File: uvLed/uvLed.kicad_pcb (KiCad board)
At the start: 2 copper layers, 71 x 9 mm, 7 parts, among them J1 Conn_01x02

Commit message: insert C
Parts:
- added C1: 100n, Capacitor_SMD:C_0805_2012Metric_Pad1.18x1.45mm_HandSolder, F.Cu at (128.7, 74.3)
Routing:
- net Net-(D4-A): track 9.19 -> 9.80 mm
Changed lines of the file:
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@@
+    )
+  )
+  (footprint "Capacitor_SMD:C_0805_2012Metric_Pad1.18x1.45mm_HandSolder" (layer "F.Cu")
+    (at 128.7 74.2625 -90)
+    (descr "Capacitor SMD 0805 (2012 Metric), square (rectangular) end terminal, IPC_7351 nominal with elongated pad for handsoldering. (Body size source: IPC-SM-782 page 76, https://www.pcb-3d.com/wordpress/wp-content/uploads/ipc-sm-782a_amendment_1_and_2.pdf, https://docs.google.com/spreadsheets/d/1BsfQQcO9C6DZCsRaXUlFlo91Tg2WpOkGARC1WS5S8t0/edit?usp=sharing), generated with kicad-footprint-generator")
+    (tags "capacitor handsolder")
+    (property "Sheetfile" "uvLed.kicad_sch")
+    (property "Sheetname" "")
+    (property "ki_description" "Unpolarized capacitor")
+    (property "ki_keywords" "cap capacitor")
+    (attr smd)
+    (fp_text reference "C1" (at 0 -1.68 90) (layer "F.SilkS")
+        (effects (font (size 1 1) (thickness 0.15)))
+    )
+    (fp_text value "100n" (at 0 1.68 90) (layer "F.Fab")
+        (effects (font (size 1 1) (thickness 0.15)))
+    )
+    (fp_text user "${REFERENCE}" (at 0 0 90) (layer "F.Fab")
+        (effects (font (size 0.5 0.5) (thickness 0.08)))
+    )
+    (fp_line (start -0.261252 -0.735) (end 0.261252 -0.735)
+      (stroke (width 0.12) (type solid)) (layer "F.SilkS"))
+    (fp_line (start -0.261252 0.735) (end 0.261252 0.735)
+      (stroke (width 0.12) (type solid)) (layer "F.SilkS"))
+    (fp_line (start -1.88 -0.98) (end 1.88 -0.98)
+      (stroke (width 0.05) (type solid)) (layer "F.CrtYd"))
+    (fp_line (start -1.88 0.98) (end -1.88 -0.98)
+      (stroke (width 0.05) (type solid)) (layer "F.CrtYd"))
+    (fp_line (start 1.88 -0.98) (end 1.88 0.98)
+      (stroke (width 0.05) (type solid)) (layer "F.CrtYd"))
+    (fp_line (start 1.88 0.98) (end -1.88 0.98)
+      (stroke (width 0.05) (type solid)) (layer "F.CrtYd"))
+    (fp_line (start -1 -0.625) (end 1 -0.625)
+      (stroke (width 0.1) (type solid)) (layer "F.Fab"))
+    (fp_line (start -1 0.625) (end -1 -0.625)
+      (stroke (width 0.1) (type solid)) (layer "F.Fab"))
+    (fp_line (start 1 -0.625) (end 1 0.625)
+      (stroke (width 0.1) (type solid)) (layer "F.Fab"))
+    (fp_line (start 1 0.625) (end -1 0.625)
+      (stroke (width 0.1) (type solid)) (layer "F.Fab"))
+    (pad "1" smd roundrect (at -1.0375 0 270) (size 1.175 1.45) (layers "F.Cu" "F.Paste" "F.Mask") (roundrect_rratio 0.212766)
+      (net 5 "Net-(D4-A)") (pintype "passive"))
+    (pad "2" smd roundrect (at 1.0375 0 270) (size 1.175 1.45) (layers "F.Cu" "F.Paste" "F.Mask") (roundrect_rratio 0.212766)
+      (net 2 "GND") (pintype "passive"))
+    (model "${KICAD6_3DMODEL_DIR}/Capacitor_SMD.3dshapes/C_0805_2012Metric.wrl"
+      (offset (xyz 0 0 0))
+      (scale (xyz 1 1 1))
+      (rotate (xyz 0 0 0))
     )
   )
@@
   (segment (start 124 75.3) (end 119 75.3) (width 0.8) (layer "F.Cu") (net 4))
   (segment (start 116.7 73) (end 112 73) (width 0.8) (layer "F.Cu") (net 4))
+  (segment (start 128.575 73.1) (end 128.7 73.225) (width 0.5) (layer "F.Cu") (net 5))
   (segment (start 133 73.46) (end 132.54 73) (width 0.8) (layer "F.Cu") (net 5))
-  (segment (start 132.54 73) (end 124 73) (width 0.8) (layer "F.Cu") (net 5))
+  (segment (start 133 73.46) (end 132.765 73.225) (width 0.8) (layer "F.Cu") (net 5))
+  (segment (start 124 73.1) (end 128.575 73.1) (width 0.5) (layer "F.Cu") (net 5))
+  (segment (start 132.765 73.225) (end 128.7 73.225) (width 0.8) (layer "F.Cu") (net 5))
   (zone (net 2) (net_name "GND") (layer "F.Cu") (hatch edge 0.5)
     (connect_pads (clearance 0.8))

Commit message: change pcb
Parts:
- moved D4 14.4 mm to (138.4, 74.0)
- moved C1 12.6 mm to (141.3, 74.2)
- moved J1 11.3 mm to (144.3, 72.9)
- moved REF** 11.0 mm to (149.0, 74.0)
- moved D3 7.70 mm to (119.7, 74.2)
- moved D2 5.90 mm to (101.9, 74.2)
- moved D1 2.10 mm to (83.1, 74.0)
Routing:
- net Net-(D3-A): track 13.0 -> 19.5 mm
- net Net-(D1-A): track 15.9 -> 19.8 mm
- net Net-(D4-A): track 9.80 -> 6.01 mm
- net Net-(D2-A): track 17.0 -> 18.7 mm
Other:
- board size 71 x 9 mm -> 81.9 x 9 mm
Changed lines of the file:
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@@
   (net 5 "Net-(D4-A)")
   (footprint "uvLED:SMD-2" (layer "F.Cu")
-    (at 124 74 90)
+    (at 138.4 74.05 90)
     (descr "LED SMD 2010 (5025 Metric), square (rectangular) end terminal, IPC_7351 nominal, (Body size source: http://www.tortai-tech.com/upload/download/2011102023233369053.pdf), generated with kicad-footprint-generator")
     (tags "LED")
@@
   )
   (footprint "MountingHole:MountingHole_2.5mm" (layer "F.Cu")
-    (at 138 74)
+    (at 149 74)
     (descr "Mounting Hole 2.5mm, no annular")
     (tags "mounting hole 2.5mm no annular")
@@
   )
   (footprint "uvLED:SMD-2" (layer "F.Cu")
-    (at 112 74 90)
+    (at 119.7 74.2 90)
     (descr "LED SMD 2010 (5025 Metric), square (rectangular) end terminal, IPC_7351 nominal, (Body size source: http://www.tortai-tech.com/upload/download/2011102023233369053.pdf), generated with kicad-footprint-generator")
     (tags "LED")
@@
   )
   (footprint "Capacitor_SMD:C_0805_2012Metric_Pad1.18x1.45mm_HandSolder" (layer "F.Cu")
-    (at 128.7 74.2625 -90)
+    (at 141.3 74.15 -90)
     (descr "Capacitor SMD 0805 (2012 Metric), square (rectangular) end terminal, IPC_7351 nominal with elongated pad for handsoldering. (Body size source: IPC-SM-782 page 76, https://www.pcb-3d.com/wordpress/wp-content/uploads/ipc-sm-782a_amendment_1_and_2.pdf, https://docs.google.com/spreadsheets/d/1BsfQQcO9C6DZCsRaXUlFlo91Tg2WpOkGARC1WS5S8t0/edit?usp=sharing), generated with kicad-footprint-generator")
     (tags "capacitor handsolder")
@@
   )
   (footprint "uvLED:SMD-2" (layer "F.Cu")
-    (at 96 74 90)
+    (at 101.9 74.2 90)
     (descr "LED SMD 2010 (5025 Metric), square (rectangular) end terminal, IPC_7351 nominal, (Body size source: http://www.tortai-tech.com/upload/download/2011102023233369053.pdf), generated with kicad-footprint-generator")
     (tags "LED")
@@
   )
   (footprint "uvLED:SMD-2" (layer "F.Cu")
-    (at 81 74 90)
+    (at 83.1 74 90)
     (descr "LED SMD 2010 (5025 Metric), square (rectangular) end terminal, IPC_7351 nominal, (Body size source: http://www.tortai-tech.com/upload/download/2011102023233369053.pdf), generated with kicad-footprint-generator")
     (tags "LED")
@@
   )
   (footprint "Connector_PinHeader_2.54mm:PinHeader_1x02_P2.54mm_Vertical" (layer "F.Cu")
-    (at 133 73.46)
+    (at 144.3 72.875)
     (descr "Through hole straight pin header, 1x02, 2.54mm pitch, single row")
     (tags "Through hole pin header THT 1x02 2.54mm single row")
@@
   (gr_line (start 70 70) (end 141 70)
     (stroke (width 0.15) (type default)) (layer "F.SilkS"))
+  (gr_line (start 141 70) (end 151.95 70)
+    (stroke (width 0.15) (type default)) (layer "F.SilkS"))
   (gr_line (start 70 79) (end 70 70)
     (stroke (width 0.15) (type default)) (layer "F.SilkS"))
   (gr_line (start 141 79) (end 70 79)
     (stroke (width 0.15) (type default)) (layer "F.SilkS"))
-  (gr_line (start 141 70) (end 141 79)
+  (gr_line (start 151.95 70) (end 151.95 79)
+    (stroke (width 0.15) (type default)) (layer "F.SilkS"))
+  (gr_line (start 141 79) (end 151.95 79)
     (stroke (width 0.15) (type default)) (layer "F.SilkS"))
   (gr_line (start 70 79) (end 70 70)
@@
   (gr_line (start 70 70) (end 141 70)
     (stroke (width 0.1) (type default)) (layer "Edge.Cuts"))
+  (gr_line (start 151.95 79) (end 141 79)
+    (stroke (width 0.1) (type default)) (layer "Edge.Cuts"))
   (gr_line (start 141 79) (end 70 79)
     (stroke (width 0.1) (type default)) (layer "Edge.Cuts"))
-  (gr_line (start 141 70) (end 141 79)
-    (stroke (width 0.1) (type default)) (layer "Edge.Cuts"))
-  (segment (start 96 75.3) (end 89.4 75.3) (width 0.8) (layer "F.Cu") (net 1))
-  (segment (start 89.4 75.3) (end 87.2 73.1) (width 0.8) (layer "F.Cu") (net 1))
-  (segment (start 87.2 73.1) (end 81 73.1) (width 0.8) (layer "F.Cu") (net 1))
-  (segment (start 102.3 75.3) (end 100 73) (width 0.8) (layer "F.Cu") (net 3))
-  (segment (start 112 75.3) (end 102.3 75.3) (width 0.8) (layer "F.Cu") (net 3))
-  (segment (start 100 73) (end 96 73) (width 0.8) (layer "F.Cu") (net 3))
-  (segment (start 119 75.3) (end 116.7 73) (width 0.8) (layer "F.Cu") (net 4))
-  (segment (start 124 75.3) (end 119 75.3) (width 0.8) (layer "F.Cu") (net 4))
-  (segment (start 116.7 73) (end 112 73) (width 0.8) (layer "F.Cu") (net 4))
-  (segment (start 128.575 73.1) (end 128.7 73.225) (width 0.5) (layer "F.Cu") (net 5))
-  (segment (start 133 73.46) (end 132.54 73) (width 0.8) (layer "F.Cu") (net 5))
-  (segment (start 133 73.46) (end 132.765 73.225) (width 0.8) (layer "F.Cu") (net 5))
-  (segment (start 124 73.1) (end 128.575 73.1) (width 0.5) (layer "F.Cu") (net 5))
-  (segment (start 132.765 73.225) (end 128.7 73.225) (width 0.8) (layer "F.Cu") (net 5))
+  (gr_line (start 151.95 70) (end 141 70)
+    (stroke (width 0.1) (type default)) (layer "Edge.Cuts"))
+  (gr_line (start 151.95 70) (end 151.95 79)
+    (stroke (width 0.1) (type default)) (layer "Edge.Cuts"))
+  (segment (start 90.4 73.1) (end 92.8 75.5) (width 0.5) (layer "F.Cu") (net 1))
+  (segment (start 92.8 75.5) (end 101.9 75.5) (width 0.5) (layer "F.Cu") (net 1))
+  (segment (start 83.1 73.1) (end 90.4 73.1) (width 0.5) (layer "F.Cu") (net 1))
+  (segment (start 111.75 75.5) (end 119.7 75.5) (width 0.5) (layer "F.Cu") (net 3))
+  (segment (start 101.9 73.3) (end 109.55 73.3) (width 0.5) (layer "F.Cu") (net 3))
+  (segment (start 109.55 73.3) (end 111.75 75.5) (width 0.5) (layer "F.Cu") (net 3))
+  (segment (start 119.7 73.3) (end 127.8 73.3) (width 0.5) (layer "F.Cu") (net 4))
+  (segment (start 127.8 73.3) (end 129.85 75.35) (width 0.5) (layer "F.Cu") (net 4))
+  (segment (start 129.85 75.35) (end 138.4 75.35) (width 0.5) (layer "F.Cu") (net 4))
+  (segment (start 141.5375 72.875) (end 141.3 73.1125) (width 0.5) (layer "F.Cu") (net 5))
+  (segment (start 138.4 73.15) (end 141.2625 73.15) (width 0.5) (layer "F.Cu") (net 5))
+  (segment (start 141.2625 73.15) (end 141.3 73.1125) (width 0.5) (layer "F.Cu") (net 5))
+  (segment (start 144.3 72.875) (end 141.5375 72.875) (width 0.5) (layer "F.Cu") (net 5))
   (zone (net 2) (net_name "GND") (layer "F.Cu") (hatch edge 0.5)
     (connect_pads (clearance 0.8))
@@
       (pts
         (xy 70 70)
-        (xy 141 70)
-        (xy 141 79)
+        (xy 152 70)
+        (xy 152 79)
         (xy 70 79)
       )

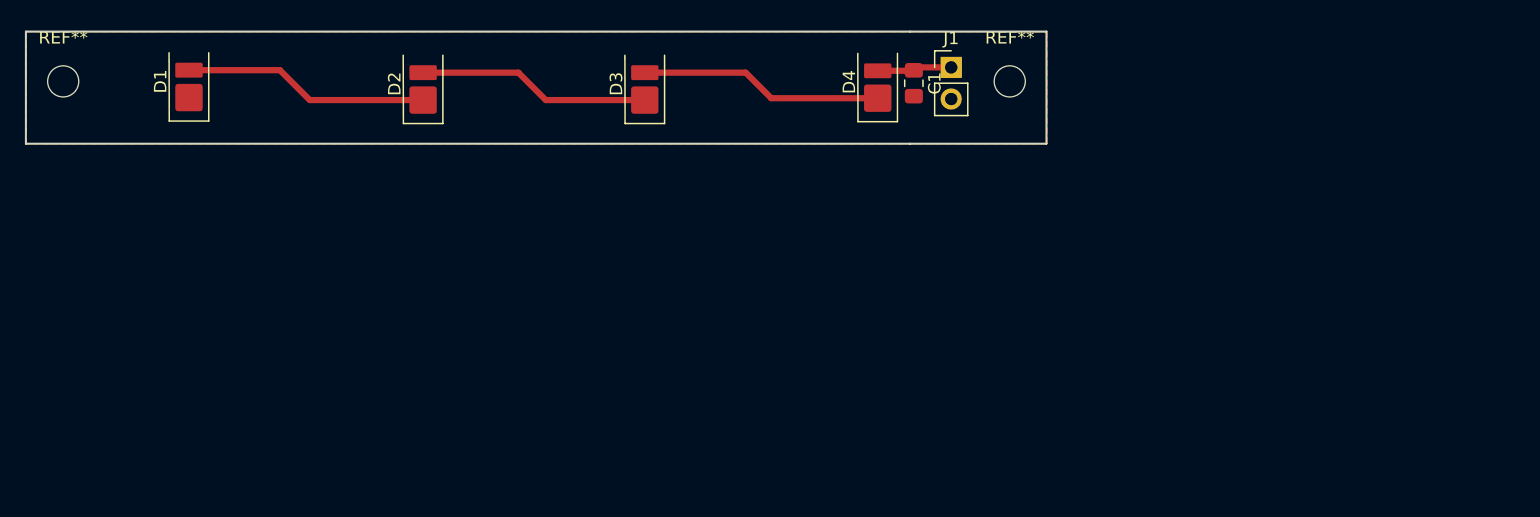
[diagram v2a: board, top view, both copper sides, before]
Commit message: Insert dimension
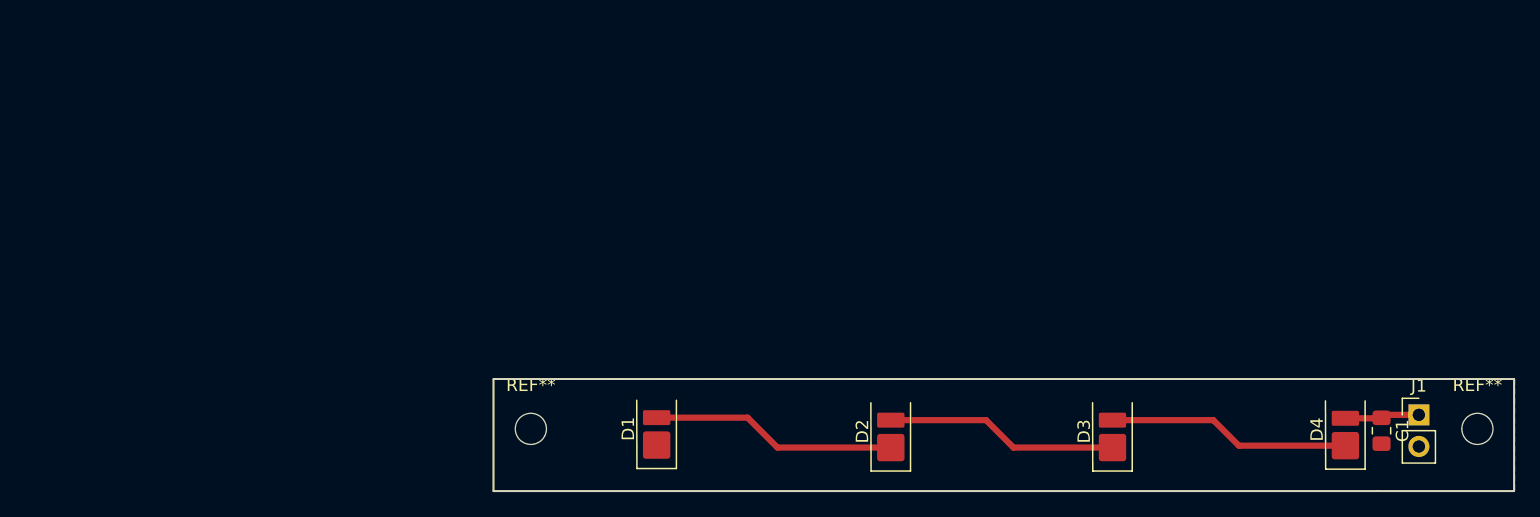
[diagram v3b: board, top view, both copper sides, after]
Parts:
- moved D1 46.8 mm to (120.7, 101.9)
- moved REF** 46.8 mm to (186.6, 101.9)
- moved REF** 46.8 mm to (110.5, 101.9)
- moved D3 46.8 mm to (157.2, 102.1)
- moved D4 46.8 mm to (175.9, 102.0)
- moved J1 46.8 mm to (181.8, 100.8)
- moved C1 46.8 mm to (178.8, 102.0)
- moved D2 46.8 mm to (139.4, 102.1)
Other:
- board size 81.9 x 9 mm -> 82 x 9 mm
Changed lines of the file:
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@@
   (net 5 "Net-(D4-A)")
   (footprint "uvLED:SMD-2" (layer "F.Cu")
-    (at 138.4 74.05 90)
+    (at 175.95 101.95 90)
     (descr "LED SMD 2010 (5025 Metric), square (rectangular) end terminal, IPC_7351 nominal, (Body size source: http://www.tortai-tech.com/upload/download/2011102023233369053.pdf), generated with kicad-footprint-generator")
     (tags "LED")
@@
   )
   (footprint "MountingHole:MountingHole_2.5mm" (layer "F.Cu")
-    (at 149 74)
+    (at 186.55 101.9)
     (descr "Mounting Hole 2.5mm, no annular")
     (tags "mounting hole 2.5mm no annular")
@@
   )
   (footprint "uvLED:SMD-2" (layer "F.Cu")
-    (at 119.7 74.2 90)
+    (at 157.25 102.1 90)
     (descr "LED SMD 2010 (5025 Metric), square (rectangular) end terminal, IPC_7351 nominal, (Body size source: http://www.tortai-tech.com/upload/download/2011102023233369053.pdf), generated with kicad-footprint-generator")
     (tags "LED")
@@
   )
   (footprint "Capacitor_SMD:C_0805_2012Metric_Pad1.18x1.45mm_HandSolder" (layer "F.Cu")
-    (at 141.3 74.15 -90)
+    (at 178.85 102.05 -90)
     (descr "Capacitor SMD 0805 (2012 Metric), square (rectangular) end terminal, IPC_7351 nominal with elongated pad for handsoldering. (Body size source: IPC-SM-782 page 76, https://www.pcb-3d.com/wordpress/wp-content/uploads/ipc-sm-782a_amendment_1_and_2.pdf, https://docs.google.com/spreadsheets/d/1BsfQQcO9C6DZCsRaXUlFlo91Tg2WpOkGARC1WS5S8t0/edit?usp=sharing), generated with kicad-footprint-generator")
     (tags "capacitor handsolder")
@@
   )
   (footprint "MountingHole:MountingHole_2.5mm" (layer "F.Cu")
-    (at 73 74)
+    (at 110.55 101.9)
     (descr "Mounting Hole 2.5mm, no annular")
     (tags "mounting hole 2.5mm no annular")
@@
   )
   (footprint "uvLED:SMD-2" (layer "F.Cu")
-    (at 101.9 74.2 90)
+    (at 139.45 102.1 90)
     (descr "LED SMD 2010 (5025 Metric), square (rectangular) end terminal, IPC_7351 nominal, (Body size source: http://www.tortai-tech.com/upload/download/2011102023233369053.pdf), generated with kicad-footprint-generator")
     (tags "LED")
@@
   )
   (footprint "uvLED:SMD-2" (layer "F.Cu")
-    (at 83.1 74 90)
+    (at 120.65 101.9 90)
     (descr "LED SMD 2010 (5025 Metric), square (rectangular) end terminal, IPC_7351 nominal, (Body size source: http://www.tortai-tech.com/upload/download/2011102023233369053.pdf), generated with kicad-footprint-generator")
     (tags "LED")
@@
   )
   (footprint "Connector_PinHeader_2.54mm:PinHeader_1x02_P2.54mm_Vertical" (layer "F.Cu")
-    (at 144.3 72.875)
+    (at 181.85 100.775)
     (descr "Through hole straight pin header, 1x02, 2.54mm pitch, single row")
     (tags "Through hole pin header THT 1x02 2.54mm single row")
@@
     )
   )
-  (gr_line (start 70 70) (end 141 70)
-    (stroke (width 0.15) (type default)) (layer "F.SilkS"))
-  (gr_line (start 141 70) (end 151.95 70)
-    (stroke (width 0.15) (type default)) (layer "F.SilkS"))
-  (gr_line (start 70 79) (end 70 70)
-    (stroke (width 0.15) (type default)) (layer "F.SilkS"))
-  (gr_line (start 141 79) (end 70 79)
-    (stroke (width 0.15) (type default)) (layer "F.SilkS"))
-  (gr_line (start 151.95 70) (end 151.95 79)
-    (stroke (width 0.15) (type default)) (layer "F.SilkS"))
-  (gr_line (start 141 79) (end 151.95 79)
-    (stroke (width 0.15) (type default)) (layer "F.SilkS"))
-  (gr_line (start 70 79) (end 70 70)
-    (stroke (width 0.1) (type default)) (layer "Edge.Cuts"))
-  (gr_line (start 70 70) (end 141 70)
-    (stroke (width 0.1) (type default)) (layer "Edge.Cuts"))
-  (gr_line (start 151.95 79) (end 141 79)
-    (stroke (width 0.1) (type default)) (layer "Edge.Cuts"))
-  (gr_line (start 141 79) (end 70 79)
-    (stroke (width 0.1) (type default)) (layer "Edge.Cuts"))
-  (gr_line (start 151.95 70) (end 141 70)
-    (stroke (width 0.1) (type default)) (layer "Edge.Cuts"))
-  (gr_line (start 151.95 70) (end 151.95 79)
-    (stroke (width 0.1) (type default)) (layer "Edge.Cuts"))
-  (segment (start 90.4 73.1) (end 92.8 75.5) (width 0.5) (layer "F.Cu") (net 1))
-  (segment (start 92.8 75.5) (end 101.9 75.5) (width 0.5) (layer "F.Cu") (net 1))
-  (segment (start 83.1 73.1) (end 90.4 73.1) (width 0.5) (layer "F.Cu") (net 1))
-  (segment (start 111.75 75.5) (end 119.7 75.5) (width 0.5) (layer "F.Cu") (net 3))
-  (segment (start 101.9 73.3) (end 109.55 73.3) (width 0.5) (layer "F.Cu") (net 3))
-  (segment (start 109.55 73.3) (end 111.75 75.5) (width 0.5) (layer "F.Cu") (net 3))
-  (segment (start 119.7 73.3) (end 127.8 73.3) (width 0.5) (layer "F.Cu") (net 4))
-  (segment (start 127.8 73.3) (end 129.85 75.35) (width 0.5) (layer "F.Cu") (net 4))
-  (segment (start 129.85 75.35) (end 138.4 75.35) (width 0.5) (layer "F.Cu") (net 4))
-  (segment (start 141.5375 72.875) (end 141.3 73.1125) (width 0.5) (layer "F.Cu") (net 5))
-  (segment (start 138.4 73.15) (end 141.2625 73.15) (width 0.5) (layer "F.Cu") (net 5))
-  (segment (start 141.2625 73.15) (end 141.3 73.1125) (width 0.5) (layer "F.Cu") (net 5))
-  (segment (start 144.3 72.875) (end 141.5375 72.875) (width 0.5) (layer "F.Cu") (net 5))
+  (gr_line (start 107.55 97.9) (end 178.55 97.9)
+    (stroke (width 0.15) (type default)) (layer "F.SilkS"))
+  (gr_line (start 178.55 97.9) (end 189.5 97.9)
+    (stroke (width 0.15) (type default)) (layer "F.SilkS"))
+  (gr_line (start 107.55 106.9) (end 107.55 97.9)
+    (stroke (width 0.15) (type default)) (layer "F.SilkS"))
+  (gr_line (start 178.55 106.9) (end 107.55 106.9)
+    (stroke (width 0.15) (type default)) (layer "F.SilkS"))
+  (gr_line (start 189.5 97.9) (end 189.5 106.9)
+    (stroke (width 0.15) (type default)) (layer "F.SilkS"))
+  (gr_line (start 178.55 106.9) (end 189.5 106.9)
+    (stroke (width 0.15) (type default)) (layer "F.SilkS"))
+  (gr_line (start 107.55 106.9) (end 107.55 97.9)
+    (stroke (width 0.1) (type default)) (layer "Edge.Cuts"))
+  (gr_line (start 107.55 97.9) (end 178.55 97.9)
+    (stroke (width 0.1) (type default)) (layer "Edge.Cuts"))
+  (gr_line (start 189.5 106.9) (end 178.55 106.9)
+    (stroke (width 0.1) (type default)) (layer "Edge.Cuts"))
+  (gr_line (start 178.55 106.9) (end 107.55 106.9)
+    (stroke (width 0.1) (type default)) (layer "Edge.Cuts"))
+  (gr_line (start 189.5 97.9) (end 178.55 97.9)
+    (stroke (width 0.1) (type default)) (layer "Edge.Cuts"))
+  (gr_line (start 189.5 97.9) (end 189.5 106.9)
+    (stroke (width 0.1) (type default)) (layer "Edge.Cuts"))
+  (dimension (type aligned) (layer "F.SilkS")
+    (pts (xy 107.55 97.9) (xy 107.55 106.9))
+    (height 8.35)
+    (gr_text "9,0000 mm" (at 98.05 102.4 90) (layer "F.SilkS")
+      (effects (font (size 1 1) (thickness 0.15)))
+    )
+    (format (prefix "") (suffix "") (units 3) (units_format 1) (precision 4))
+    (style (thickness 0.15) (arrow_length 1.27) (text_position_mode 0) (extension_height 0.58642) (extension_offset 0.5) keep_text_aligned)
+  )
+  (dimension (type aligned) (layer "F.SilkS")
+    (pts (xy 107.55 97.9) (xy 189.55 97.9))
+    (height -6.5)
+    (gr_text "82,0000 mm" (at 148.55 90.25) (layer "F.SilkS")
+      (effects (font (size 1 1) (thickness 0.15)))
+    )
+    (format (prefix "") (suffix "") (units 3) (units_format 1) (precision 4))
+    (style (thickness 0.15) (arrow_length 1.27) (text_position_mode 0) (extension_height 0.58642) (extension_offset 0.5) keep_text_aligned)
+  )
+  (segment (start 127.95 101) (end 130.35 103.4) (width 0.5) (layer "F.Cu") (net 1))
+  (segment (start 130.35 103.4) (end 139.45 103.4) (width 0.5) (layer "F.Cu") (net 1))
+  (segment (start 120.65 101) (end 127.95 101) (width 0.5) (layer "F.Cu") (net 1))
+  (segment (start 149.3 103.4) (end 157.25 103.4) (width 0.5) (layer "F.Cu") (net 3))
+  (segment (start 139.45 101.2) (end 147.1 101.2) (width 0.5) (layer "F.Cu") (net 3))
+  (segment (start 147.1 101.2) (end 149.3 103.4) (width 0.5) (layer "F.Cu") (net 3))
+  (segment (start 157.25 101.2) (end 165.35 101.2) (width 0.5) (layer "F.Cu") (net 4))
+  (segment (start 165.35 101.2) (end 167.4 103.25) (width 0.5) (layer "F.Cu") (net 4))
+  (segment (start 167.4 103.25) (end 175.95 103.25) (width 0.5) (layer "F.Cu") (net 4))
+  (segment (start 179.0875 100.775) (end 178.85 101.0125) (width 0.5) (layer "F.Cu") (net 5))
+  (segment (start 175.95 101.05) (end 178.8125 101.05) (width 0.5) (layer "F.Cu") (net 5))
+  (segment (start 178.8125 101.05) (end 178.85 101.0125) (width 0.5) (layer "F.Cu") (net 5))
+  (segment (start 181.85 100.775) (end 179.0875 100.775) (width 0.5) (layer "F.Cu") (net 5))
   (zone (net 2) (net_name "GND") (layer "F.Cu") (hatch edge 0.5)
     (connect_pads (clearance 0.8))
@@
     (polygon
       (pts
-        (xy 70 70)
-        (xy 152 70)
-        (xy 152 79)
-        (xy 70 79)
+        (xy 107.55 97.9)
+        (xy 189.55 97.9)
+        (xy 189.55 106.9)
+        (xy 107.55 106.9)
       )
     )
